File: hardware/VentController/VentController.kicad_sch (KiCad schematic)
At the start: 1 part

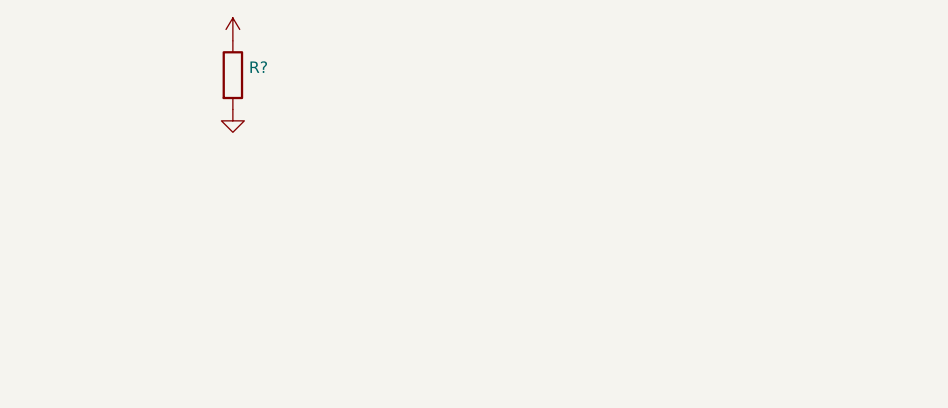
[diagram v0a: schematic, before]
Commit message: Add power plane to schematic
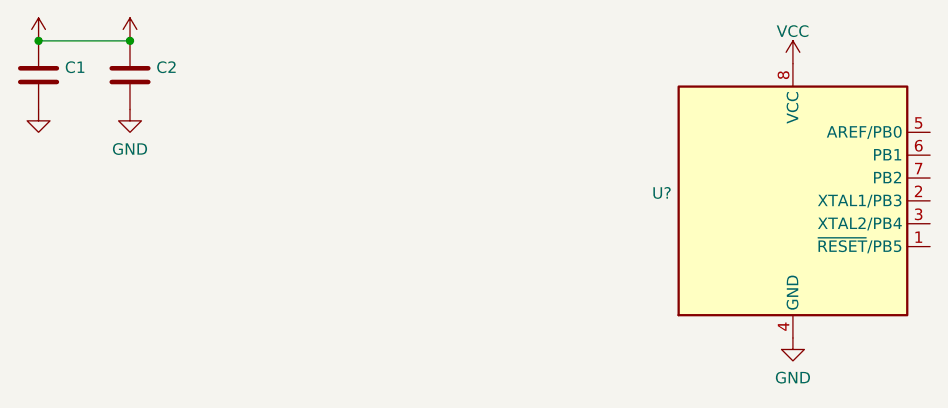
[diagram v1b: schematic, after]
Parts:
- removed R?: (no value), symbol Device:R
- added C1, C2: (no value), symbol Device:C
- added U?: (no value), symbol MCU_Microchip_ATtiny:ATtiny85-20P
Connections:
- net GND: now also C1.2, C2.2, U?.4 (GND)
- new net +5V: C1.1, C2.1, U?.8 (VCC)
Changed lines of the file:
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@@
 (kicad_sch (version 20211123) (generator eeschema)
   (paper "A4")
-  (symbol (lib_id "Device:R") (at 71.12 77.47 0) (unit 1)
+  (junction (at 59.69 73.66) (diameter 0) (color 0 0 0 0)
+  )
+  (junction (at 49.53 73.66) (diameter 0) (color 0 0 0 0)
+  )
+  (wire (pts (xy 49.53 73.66) (xy 59.69 73.66))
+    (stroke (width 0) (type default) (color 0 0 0 0))
+  )
+  (symbol (lib_id "power:GND") (at 49.53 81.28 0) (unit 1)
     (in_bom yes) (on_board yes) (fields_autoplaced)
-    (property "Reference" "R?" (id 0) (at 72.898 76.6353 0)
+    (property "Reference" "#PWR02" (id 0) (at 49.53 87.63 0)
+      (effects (font (size 1.27 1.27)) hide)
+    )
+    (property "Value" "" (id 1) (at 49.53 85.7234 0))
+    (property "Footprint" "" (id 2) (at 49.53 81.28 0)
+      (effects (font (size 1.27 1.27)) hide)
+    )
+    (property "Datasheet" "" (id 3) (at 49.53 81.28 0)
+      (effects (font (size 1.27 1.27)) hide)
+    )
+    (pin "1")
+  )
+  (symbol (lib_id "power:GND") (at 133.35 106.68 0) (unit 1)
+    (in_bom yes) (on_board yes) (fields_autoplaced)
+    (property "Reference" "#PWR?" (id 0) (at 133.35 113.03 0)
+      (effects (font (size 1.27 1.27)) hide)
+    )
+    (property "Value" "GND" (id 1) (at 133.35 111.1234 0))
+    (property "Footprint" "" (id 2) (at 133.35 106.68 0)
+      (effects (font (size 1.27 1.27)) hide)
+    )
+    (property "Datasheet" "" (id 3) (at 133.35 106.68 0)
+      (effects (font (size 1.27 1.27)) hide)
+    )
+    (pin "1")
+  )
+  (symbol (lib_id "power:VCC") (at 133.35 76.2 0) (unit 1)
+    (in_bom yes) (on_board yes) (fields_autoplaced)
+    (property "Reference" "#PWR?" (id 0) (at 133.35 80.01 0)
+      (effects (font (size 1.27 1.27)) hide)
+    )
+    (property "Value" "VCC" (id 1) (at 133.35 72.6242 0))
+    (property "Footprint" "" (id 2) (at 133.35 76.2 0)
+      (effects (font (size 1.27 1.27)) hide)
+    )
+    (property "Datasheet" "" (id 3) (at 133.35 76.2 0)
+      (effects (font (size 1.27 1.27)) hide)
+    )
+    (pin "1")
+  )
+  (symbol (lib_id "power:GND") (at 59.69 81.28 0) (unit 1)
+    (in_bom yes) (on_board yes) (fields_autoplaced)
+    (property "Reference" "#PWR04" (id 0) (at 59.69 87.63 0)
+      (effects (font (size 1.27 1.27)) hide)
+    )
+    (property "Value" "GND" (id 1) (at 59.69 85.7234 0))
+    (property "Footprint" "" (id 2) (at 59.69 81.28 0)
+      (effects (font (size 1.27 1.27)) hide)
+    )
+    (property "Datasheet" "" (id 3) (at 59.69 81.28 0)
+      (effects (font (size 1.27 1.27)) hide)
+    )
+    (pin "1")
+  )
+  (symbol (lib_id "power:+5V") (at 49.53 73.66 0) (unit 1)
+    (in_bom yes) (on_board yes) (fields_autoplaced)
+    (property "Reference" "#PWR01" (id 0) (at 49.53 77.47 0)
+      (effects (font (size 1.27 1.27)) hide)
+    )
+    (property "Value" "" (id 1) (at 49.53 70.0842 0))
+    (property "Footprint" "" (id 2) (at 49.53 73.66 0)
+      (effects (font (size 1.27 1.27)) hide)
+    )
+    (property "Datasheet" "" (id 3) (at 49.53 73.66 0)
+      (effects (font (size 1.27 1.27)) hide)
+    )
+    (pin "1")
+  )
+  (symbol (lib_id "MCU_Microchip_ATtiny:ATtiny85-20P") (at 133.35 91.44 0) (unit 1)
+    (in_bom yes) (on_board yes) (fields_autoplaced)
+    (property "Reference" "U?" (id 0) (at 119.888 90.6053 0)
+      (effects (font (size 1.27 1.27)) (justify right))
+    )
+    (property "Value" "" (id 1) (at 119.888 93.1422 0)
+      (effects (font (size 1.27 1.27)) (justify right))
+    )
+    (property "Footprint" "" (id 2) (at 133.35 91.44 0)
+      (effects (font (size 1.27 1.27) italic) hide)
+    )
+    (property "Datasheet" "http://ww1.microchip.com/downloads/en/DeviceDoc/atmel-2586-avr-8-bit-microcontroller-attiny25-attiny45-attiny85_datasheet.pdf" (id 3) (at 133.35 91.44 0)
+      (effects (font (size 1.27 1.27)) hide)
+    )
+    (pin "1")
+    (pin "2")
+    (pin "3")
+    (pin "4")
+    (pin "5")
+    (pin "6")
+    (pin "7")
+    (pin "8")
+  )
+  (symbol (lib_id "power:VCC") (at 59.69 73.66 0) (unit 1)
+    (in_bom yes) (on_board yes) (fields_autoplaced)
+    (property "Reference" "#PWR03" (id 0) (at 59.69 77.47 0)
+      (effects (font (size 1.27 1.27)) hide)
+    )
+    (property "Value" "" (id 1) (at 59.69 70.0842 0))
+    (property "Footprint" "" (id 2) (at 59.69 73.66 0)
+      (effects (font (size 1.27 1.27)) hide)
+    )
+    (property "Datasheet" "" (id 3) (at 59.69 73.66 0)
+      (effects (font (size 1.27 1.27)) hide)
+    )
+    (pin "1")
+  )
+  (symbol (lib_id "Device:C") (at 59.69 77.47 0) (unit 1)
+    (in_bom yes) (on_board yes) (fields_autoplaced)
+    (property "Reference" "C2" (id 0) (at 62.611 76.6353 0)
       (effects (font (size 1.27 1.27)) (justify left))
     )
-    (property "Value" "" (id 1) (at 72.898 79.1722 0)
+    (property "Value" "" (id 1) (at 62.611 79.1722 0)
       (effects (font (size 1.27 1.27)) (justify left))
     )
-    (property "Footprint" "" (id 2) (at 69.342 77.47 90)
+    (property "Footprint" "" (id 2) (at 60.6552 81.28 0)
       (effects (font (size 1.27 1.27)) hide)
     )
-    (property "Datasheet" "~" (id 3) (at 71.12 77.47 0)
+    (property "Datasheet" "~" (id 3) (at 59.69 77.47 0)
       (effects (font (size 1.27 1.27)) hide)
     )
@@
     (pin "2")
   )
-  (symbol (lib_id "power:GND") (at 71.12 81.28 0) (unit 1)
+  (symbol (lib_id "Device:C") (at 49.53 77.47 0) (unit 1)
     (in_bom yes) (on_board yes) (fields_autoplaced)
-    (property "Reference" "#PWR?" (id 0) (at 71.12 87.63 0)
+    (property "Reference" "C1" (id 0) (at 52.451 76.6353 0)
+      (effects (font (size 1.27 1.27)) (justify left))
+    )
+    (property "Value" "" (id 1) (at 52.451 79.1722 0)
+      (effects (font (size 1.27 1.27)) (justify left))
+    )
+    (property "Footprint" "" (id 2) (at 50.4952 81.28 0)
       (effects (font (size 1.27 1.27)) hide)
     )
-    (property "Value" "" (id 1) (at 71.12 85.7234 0))
-    (property "Footprint" "" (id 2) (at 71.12 81.28 0)
-      (effects (font (size 1.27 1.27)) hide)
-    )
-    (property "Datasheet" "" (id 3) (at 71.12 81.28 0)
+    (property "Datasheet" "~" (id 3) (at 49.53 77.47 0)
       (effects (font (size 1.27 1.27)) hide)
     )
     (pin "1")
-  )
-  (symbol (lib_id "power:VCC") (at 71.12 73.66 0) (unit 1)
-    (in_bom yes) (on_board yes) (fields_autoplaced)
-    (property "Reference" "#PWR?" (id 0) (at 71.12 77.47 0)
-      (effects (font (size 1.27 1.27)) hide)
-    )
-    (property "Value" "" (id 1) (at 71.12 70.0842 0))
-    (property "Footprint" "" (id 2) (at 71.12 73.66 0)
-      (effects (font (size 1.27 1.27)) hide)
-    )
-    (property "Datasheet" "" (id 3) (at 71.12 73.66 0)
-      (effects (font (size 1.27 1.27)) hide)
-    )
-    (pin "1")
+    (pin "2")
   )
   (sheet_instances
@@
   )
   (symbol_instances
+    (path "/4bc7e3b2-58d4-489c-bd7b-7434fdcc1337"
+      (reference "#PWR01") (unit 1) (value "+5V") (footprint "")
+    )
     (path "/09682f05-b4e6-4e50-98a0-ce1e14e1d9ed"
+      (reference "#PWR02") (unit 1) (value "GND") (footprint "")
+    )
+    (path "/700baee8-660b-46d3-860e-6faae63eba8c"
+      (reference "#PWR03") (unit 1) (value "VCC") (footprint "")
+    )
+    (path "/49996e5f-2048-45fb-b7cb-320f2acfcff1"
+      (reference "#PWR04") (unit 1) (value "GND") (footprint "")
+    )
+    (path "/12c8cfe2-5aef-4a5c-90e3-4338cb8ce58d"
       (reference "#PWR?") (unit 1) (value "GND") (footprint "")
     )
-    (path "/8c4cd1a2-9a92-4fba-aa2e-8b86c17dce10"
+    (path "/48fc5427-1512-4941-ab0c-806b9c67cc3f"
       (reference "#PWR?") (unit 1) (value "VCC") (footprint "")
     )
-    (path "/092f439c-150d-415b-8b93-adf5f43b88bb"
-      (reference "R?") (unit 1) (value "R") (footprint "")
+    (path "/f81e2caa-f7a2-40dd-8668-c447b8223c0a"
+      (reference "C1") (unit 1) (value "1uF") (footprint "")
+    )
+    (path "/84d51517-c996-417b-a237-4ad19d974db6"
+      (reference "C2") (unit 1) (value ".1uF") (footprint "")
+    )
+    (path "/5191bbb8-5f55-42b2-8d86-545a41a42ad9"
+      (reference "U?") (unit 1) (value "ATtiny85-20P") (footprint "Package_DIP:DIP-8_W7.62mm")
     )
   )

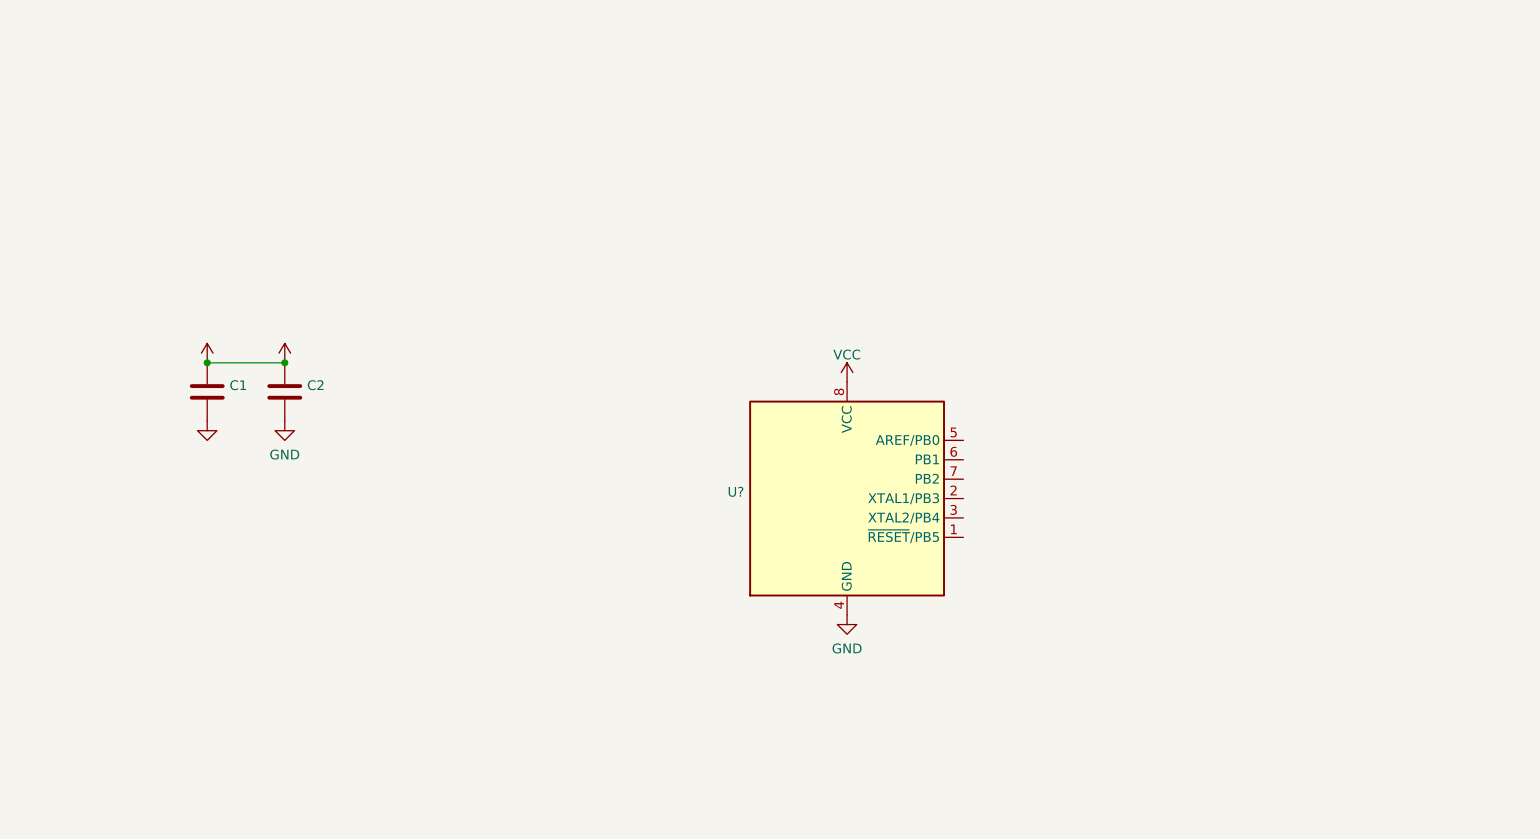
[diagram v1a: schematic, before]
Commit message: Add controller layout
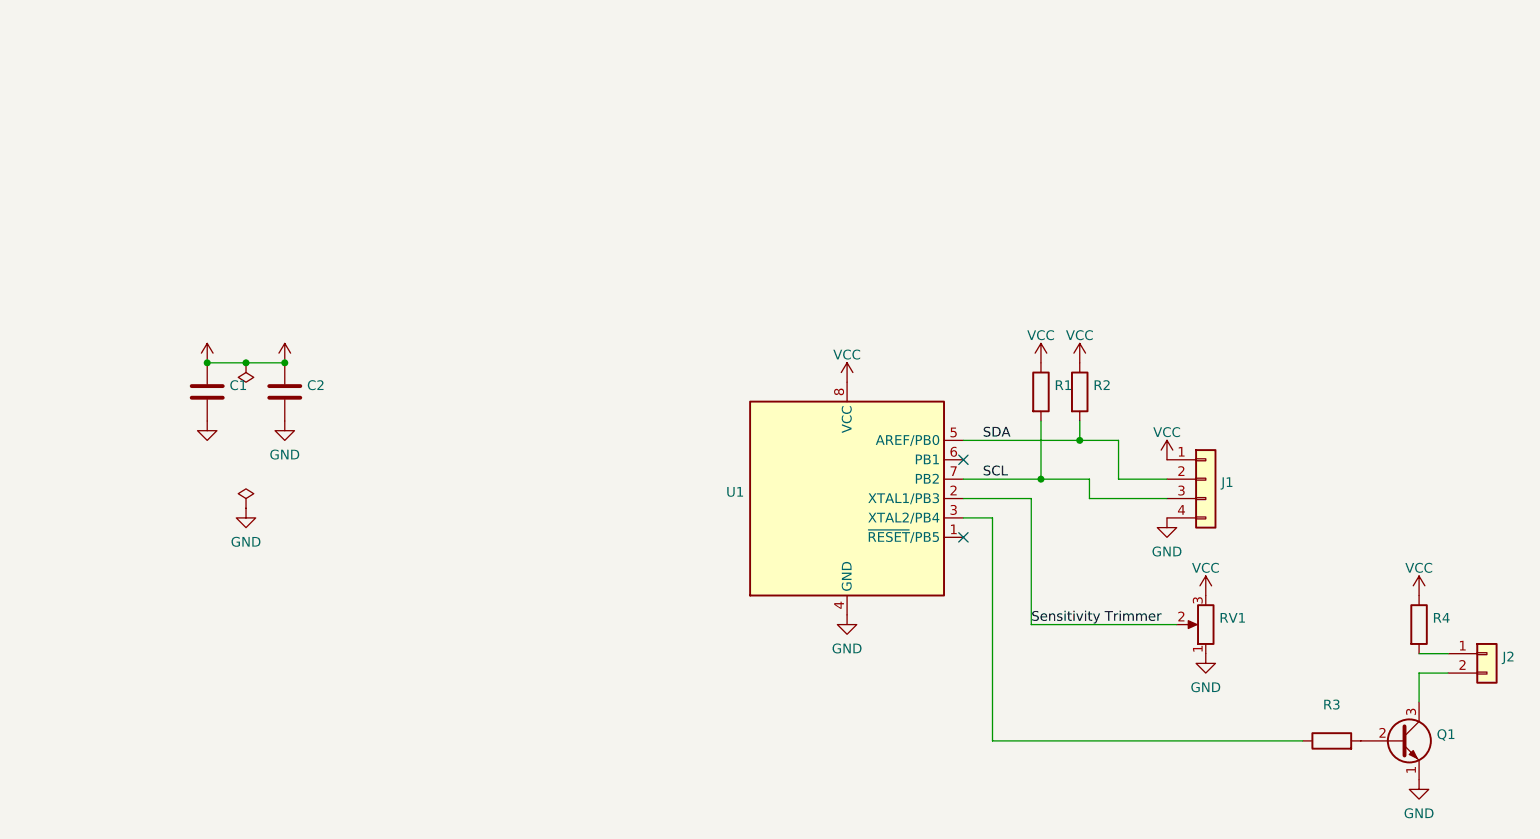
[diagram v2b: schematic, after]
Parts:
- added J1: (no value), symbol Connector_Generic:Conn_01x04
- added J2: (no value), symbol Connector_Generic:Conn_01x02
- added Q1: (no value), symbol Device:Q_NPN_EBC
- added R1, R2, R3, R4: (no value), symbol Device:R
- added RV1: (no value), symbol Device:R_Potentiometer
- gave numbers to parts that had none: 1
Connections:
- net +5V: now also J1.1 (Pin_1), R1.1, R2.1, R4.1, RV1.3
- net GND: now also J1.4 (Pin_4), Q1.1 (E), RV1.1
- net Sensitivity Trimmer: now reaches U1.2 (XTAL1/PB3)
- net Sensitivity Trimmer: now also RV1.2
- net at U1.3 (XTAL2/PB4): now also R3.1
- net SDA: now reaches U1.5 (AREF/PB0)
- net SDA: now also J1.2 (Pin_2), R2.2
- net SCL: now reaches U1.7 (PB2)
- net SCL: now also J1.3 (Pin_3), R1.2
- new net: Q1.2 (B), R3.2
- new net: J2.1 (Pin_1), R4.2
- new net: J2.2 (Pin_2), Q1.3 (C)
- no-connect marks 0 -> 2

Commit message: Add ssr25 decoupling cap
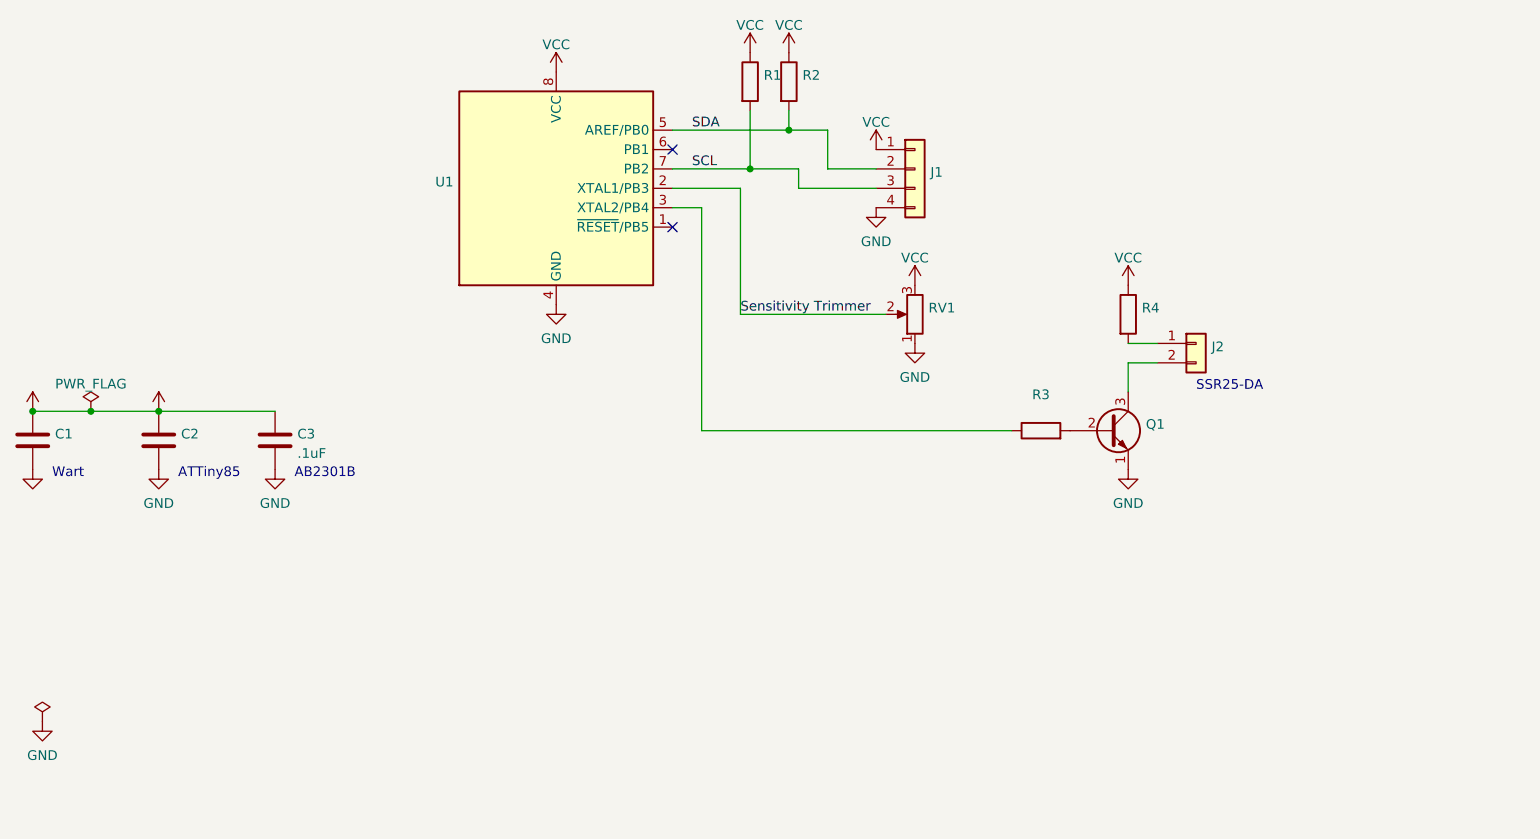
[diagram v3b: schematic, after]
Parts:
- added C3: .1uF, symbol Device:C
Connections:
- net +5V: now also C3.1
- net GND: now also C3.2
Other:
- note added: "AB2301B"
- note added: "ATTiny85"
- note added: "SSR25-DA"
- note added: "Wart"
- title: (none) -> VentController
- moved on the sheet: C1, C2, J1, J2, Q1, R1, R2, R3, R4, RV1, U1
